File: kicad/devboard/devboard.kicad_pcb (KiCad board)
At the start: 2 copper layers, 4 parts, among them U2 CH340G, U3 STM32G030K8Tx

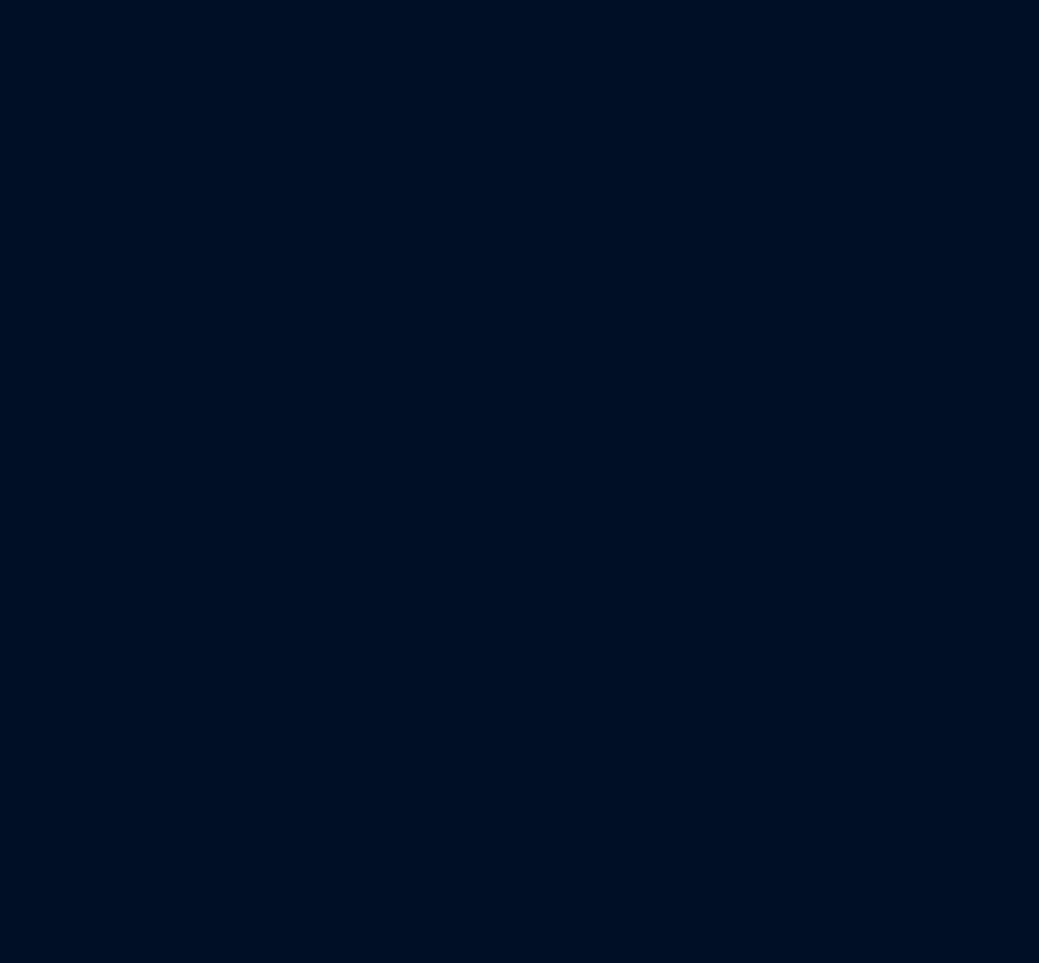
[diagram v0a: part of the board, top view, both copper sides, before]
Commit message: Added pin headers for SWD
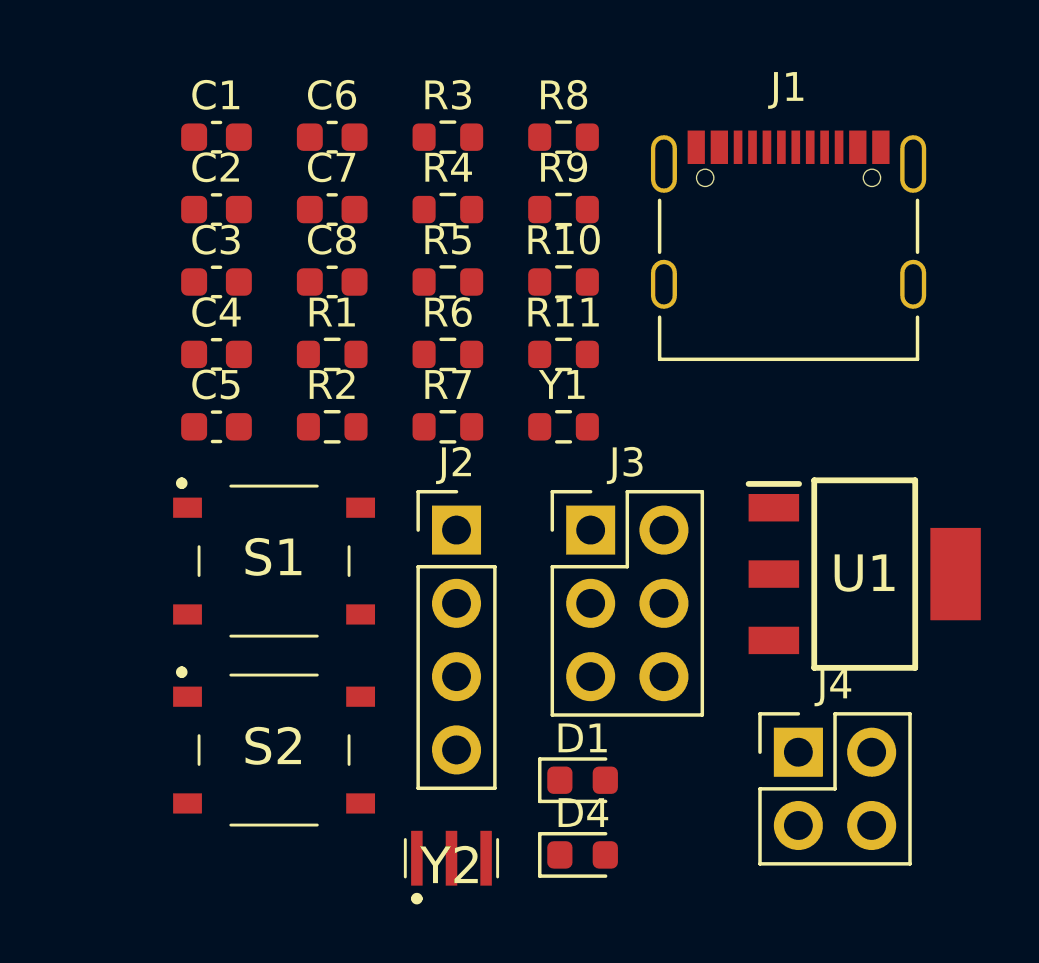
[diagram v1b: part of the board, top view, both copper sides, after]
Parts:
- added C1: 0.47 uF, Capacitor_SMD:C_0603_1608Metric, F.Cu at (138.3, 48.6)
- added C2: 33 uF, Capacitor_SMD:C_0603_1608Metric, F.Cu at (138.3, 51.1)
- added C3: 22 pF, Capacitor_SMD:C_0603_1608Metric, F.Cu at (138.3, 53.7)
- added C4: 22 pF, Capacitor_SMD:C_0603_1608Metric, F.Cu at (138.3, 56.2)
- added C5: 100 nF, Capacitor_SMD:C_0603_1608Metric, F.Cu at (138.3, 58.7)
- added C6: 0.1 uF, Capacitor_SMD:C_0603_1608Metric, F.Cu at (142.3, 48.6)
- added C7: 100 nF, Capacitor_SMD:C_0603_1608Metric, F.Cu at (142.3, 51.1)
- added C8: 100 nF, Capacitor_SMD:C_0603_1608Metric, F.Cu at (142.3, 53.7)
- added D1: LED, LED_SMD:LED_0603_1608Metric, F.Cu at (151.0, 70.9)
- added D4: LED, LED_SMD:LED_0603_1608Metric, F.Cu at (151.0, 73.5)
- added J1: USB_C_Receptacle, Connector_USB:USB_C_Receptacle_Palconn_UTC16-G, F.Cu at (158.1, 51.5)
- added J2: Conn_01x04_Socket, Connector_PinHeader_2.54mm:PinHeader_1x04_P2.54mm_Vertical, F.Cu at (146.6, 62.3)
- added J3: Conn_02x03_Top_Bottom, Connector_PinHeader_2.54mm:PinHeader_2x03_P2.54mm_Vertical, F.Cu at (151.3, 62.3)
- added J4: Conn_02x02_Top_Bottom, Connector_PinHeader_2.54mm:PinHeader_2x02_P2.54mm_Vertical, F.Cu at (158.5, 70.0)
- added R1: 1M, Resistor_SMD:R_0603_1608Metric, F.Cu at (142.3, 56.2)
- added R10: 10k, Resistor_SMD:R_0603_1608Metric, F.Cu at (150.3, 53.7)
- added R11: 10k, Resistor_SMD:R_0603_1608Metric, F.Cu at (150.3, 56.2)
- added R2: 1k, Resistor_SMD:R_0603_1608Metric, F.Cu at (142.3, 58.7)
- added R3: 470, Resistor_SMD:R_0603_1608Metric, F.Cu at (146.3, 48.6)
- added R4: 10k, Resistor_SMD:R_0603_1608Metric, F.Cu at (146.3, 51.1)
- added R5: 603, Resistor_SMD:R_0603_1608Metric, F.Cu at (146.3, 53.7)
- added R6: 5k1, Resistor_SMD:R_0603_1608Metric, F.Cu at (146.3, 56.2)
- added R7: 5k1, Resistor_SMD:R_0603_1608Metric, F.Cu at (146.3, 58.7)
- added R8: 1k, Resistor_SMD:R_0603_1608Metric, F.Cu at (150.3, 48.6)
- added R9: 1k, Resistor_SMD:R_0603_1608Metric, F.Cu at (150.3, 51.1)
- added S1: ~, mesonlib:PTS526SM15SMTR2LFS, F.Cu at (140.3, 63.3)
- added S2: ~, mesonlib:PTS526SM15SMTR2LFS, F.Cu at (140.3, 69.9)
- added U1: LM3940, mesonlib:LM3940, F.Cu at (160.8, 63.8)
- added Y1: 12 MHz, Resistor_SMD:R_0603_1608Metric, F.Cu at (150.3, 58.7)
- added Y2: 8 MHz, mesonlib:CSTNE16M0V530000R0, F.Cu at (146.4, 74.1)
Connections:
- U3 pad 19: Net-(U2-TXD) -> /TX-M
- U3 pad 21: Net-(U2-RXD) -> /RX-M
- U3 pad 24: unconnected-(U3-PA13-Pad24) -> /SWDIO

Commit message: All footprints done?
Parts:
- added C9: EEU-FR1V330, mesonlib:EEU-FR1330, F.Cu at (125.5, 85.3)
- added TH1: Thermistor_PTC, mesonlib:Eaton PTS120616V025, F.Cu at (135.5, 89.0)
- D1, D4, J1, S1, S2: moved to B.Cu
- Y1: footprint Resistor_SMD:R_0603_1608Metric -> Crystal:Crystal_SMD_HC49-SD
- moved Y1 28.3 mm to (178.6, 58.4)
- moved U1 16.7 mm to (177.2, 66.5)
- moved J3 9.94 mm to (159.7, 67.5)
- moved J4 9.35 mm to (159.7, 79.2)
- moved S1 8.37 mm to (132.0, 64.5), turned to 180 degrees
- moved Y2 7.61 mm to (144.5, 81.4)
- moved S2 7.02 mm to (135.0, 74.5), turned to 180 degrees
- moved D1 6.08 mm to (153.7, 65.5), turned to 180 degrees
- moved D4 4.27 mm to (154.0, 70.5), turned to 180 degrees
- moved J2 4.19 mm to (150.5, 60.7)
- moved J1 4.13 mm to (162.2, 50.8), turned to 180 degrees
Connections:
- net /BOOT renamed /SWCLK/BOOT

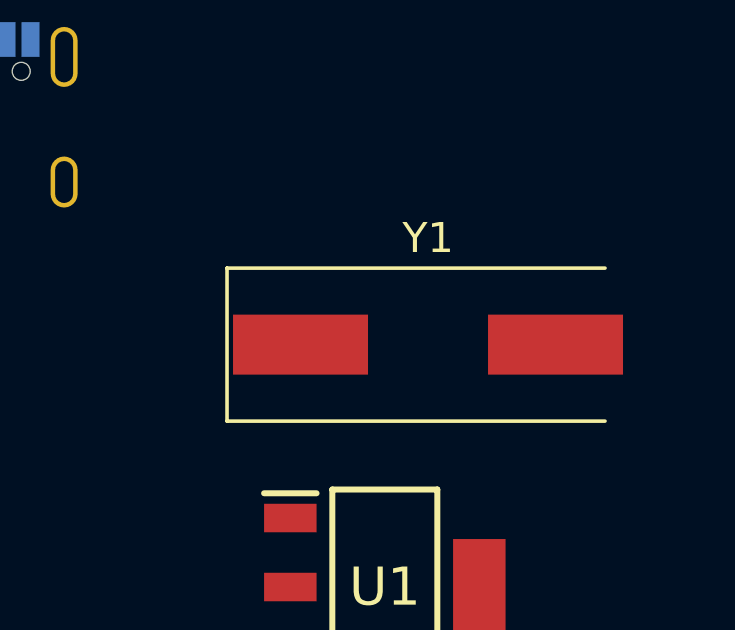
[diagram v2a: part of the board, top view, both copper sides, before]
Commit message: Added new 16-pin USB C symbol, updated PCB
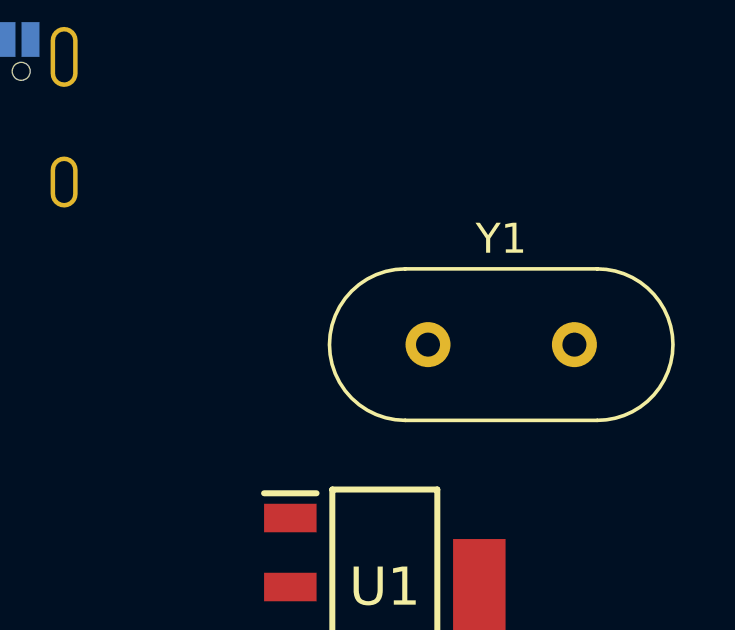
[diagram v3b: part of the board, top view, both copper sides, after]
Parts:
- Y1: footprint Crystal:Crystal_SMD_HC49-SD -> Crystal:Crystal_HC49-4H_Vertical
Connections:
- U1 pad 4: (no net) -> GND
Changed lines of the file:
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@@
 		)
 	)
-	(footprint "Crystal:Crystal_SMD_HC49-SD"
+	(footprint "Crystal:Crystal_HC49-4H_Vertical"
 		(layer "F.Cu")
 		(at 178.63 58.42)
-		(descr "SMD Crystal HC-49-SD http://cdn-reichelt.de/documents/datenblatt/B400/xxx-HC49-SMD.pdf, 11.4x4.7mm^2 package")
-		(tags "SMD SMT crystal")
+		(descr "Crystal THT HC-49-4H http://5hertz.com/pdfs/04404_D.pdf")
+		(tags "THT crystalHC-49-4H")
 		(property "Reference" "Y1"
-			(at 0 -3.55 0)
+			(at 2.44 -3.525 0)
 			(layer "F.SilkS")
 			(effects
@@
 		)
 		(property "Value" "12 MHz	"
-			(at 0 3.55 0)
+			(at 2.44 3.525 0)
 			(layer "F.Fab")
 			(effects
@@
 			)
 		)
-		(property "Footprint" "Crystal:Crystal_SMD_HC49-SD"
+		(property "Footprint" "Crystal:Crystal_HC49-4H_Vertical"
 			(at 0 0 0)
 			(unlocked yes)
@@
 		(sheetname "Root")
 		(sheetfile "devboard.kicad_sch")
-		(attr smd)
+		(attr through_hole)
 		(fp_line
-			(start -6.7 -2.55)
-			(end -6.7 2.55)
+			(start -0.76 -2.525)
+			(end 5.64 -2.525)
 			(stroke
 				(width 0.12)
@@
 		)
 		(fp_line
-			(start -6.7 2.55)
-			(end 5.9 2.55)
+			(start -0.76 2.525)
+			(end 5.64 2.525)
 			(stroke
 				(width 0.12)
@@
 			(layer "F.SilkS")
 		)
-		(fp_line
-			(start 5.9 -2.55)
-			(end -6.7 -2.55)
+		(fp_arc
+			(start -0.76 2.525)
+			(mid -3.285 0)
+			(end -0.76 -2.525)
+			(stroke
+				(width 0.12)
+				(type solid)
+			)
+			(layer "F.SilkS")
+		)
+		(fp_arc
+			(start 5.64 -2.525)
+			(mid 8.165 0)
+			(end 5.64 2.525)
 			(stroke
 				(width 0.12)
@@
 		)
 		(fp_line
-			(start -6.8 -2.6)
-			(end -6.8 2.6)
+			(start -3.6 -2.8)
+			(end -3.6 2.8)
 			(stroke
 				(width 0.05)
@@
 		)
 		(fp_line
-			(start -6.8 2.6)
-			(end 6.8 2.6)
+			(start -3.6 2.8)
+			(end 8.5 2.8)
 			(stroke
 				(width 0.05)
@@
 		)
 		(fp_line
-			(start 6.8 -2.6)
-			(end -6.8 -2.6)
+			(start 8.5 -2.8)
+			(end -3.6 -2.8)
 			(stroke
 				(width 0.05)
@@
 		)
 		(fp_line
-			(start 6.8 2.6)
-			(end 6.8 -2.6)
+			(start 8.5 2.8)
+			(end 8.5 -2.8)
 			(stroke
 				(width 0.05)
@@
 		)
 		(fp_line
-			(start -5.7 -2.35)
-			(end -5.7 2.35)
+			(start -0.76 -2.325)
+			(end 5.64 -2.325)
 			(stroke
 				(width 0.1)
@@
 		)
 		(fp_line
-			(start -5.7 2.35)
-			(end 5.7 2.35)
+			(start -0.76 2.325)
+			(end 5.64 2.325)
 			(stroke
 				(width 0.1)
@@
 		)
 		(fp_line
-			(start -3.015 -2.115)
-			(end 3.015 -2.115)
+			(start -0.56 -2)
+			(end 5.44 -2)
 			(stroke
 				(width 0.1)
@@
 		)
 		(fp_line
-			(start -3.015 2.115)
-			(end 3.015 2.115)
+			(start -0.56 2)
+			(end 5.44 2)
 			(stroke
 				(width 0.1)
@@
 			(layer "F.Fab")
 		)
-		(fp_line
-			(start 5.7 -2.35)
-			(end -5.7 -2.35)
+		(fp_arc
+			(start -0.76 2.325)
+			(mid -3.085 0)
+			(end -0.76 -2.325)
 			(stroke
 				(width 0.1)
@@
 			(layer "F.Fab")
 		)
-		(fp_line
-			(start 5.7 2.35)
-			(end 5.7 -2.35)
+		(fp_arc
+			(start -0.56 2)
+			(mid -2.56 0)
+			(end -0.56 -2)
 			(stroke
 				(width 0.1)
@@
 		)
 		(fp_arc
-			(start -3.015 2.115)
-			(mid -5.13 0)
-			(end -3.015 -2.115)
+			(start 5.44 -2)
+			(mid 7.44 0)
+			(end 5.44 2)
 			(stroke
 				(width 0.1)
@@
 		)
 		(fp_arc
-			(start 3.015 -2.115)
-			(mid 5.13 0)
-			(end 3.015 2.115)
+			(start 5.64 -2.325)
+			(mid 7.965 0)
+			(end 5.64 2.325)
 			(stroke
 				(width 0.1)
@@
 		)
 		(fp_text user "${REFERENCE}"
-			(at 0 0 0)
+			(at 2.44 0 0)
 			(layer "F.Fab")
 			(effects
@@
 			)
 		)
-		(pad "1" smd rect
-			(at -4.25 0)
-			(size 4.5 2)
-			(layers "F.Cu" "F.Paste" "F.Mask")
+		(pad "1" thru_hole circle
+			(at 0 0)
+			(size 1.5 1.5)
+			(drill 0.8)
+			(layers "*.Cu" "*.Mask")
+			(remove_unused_layers no)
 			(net 19 "Net-(U2-XI)")
 			(pinfunction "1")
 			(pintype "passive")
 		)
-		(pad "2" smd rect
-			(at 4.25 0)
-			(size 4.5 2)
-			(layers "F.Cu" "F.Paste" "F.Mask")
+		(pad "2" thru_hole circle
+			(at 4.88 0)
+			(size 1.5 1.5)
+			(drill 0.8)
+			(layers "*.Cu" "*.Mask")
+			(remove_unused_layers no)
 			(net 8 "Net-(U2-XO)")
 			(pinfunction "2")
 			(pintype "passive")
 		)
-		(model "${KICAD8_3DMODEL_DIR}/Crystal.3dshapes/Crystal_SMD_HC49-SD.wrl"
+		(model "${KICAD8_3DMODEL_DIR}/Crystal.3dshapes/Crystal_HC49-4H_Vertical.wrl"
 			(offset
 				(xyz 0 0 0)
@@
 			(size 1.75 3.2)
 			(layers "F.Cu" "F.Paste" "F.Mask")
+			(net 3 "GND")
+			(pintype "passive")
 			(thermal_bridge_angle 45)
 		)
@@
 		(tags "LED")
 		(property "Reference" "D1"
-			(at 0 1.43 -180)
+			(at 0 1.43 180)
 			(layer "B.SilkS")
 			(effects

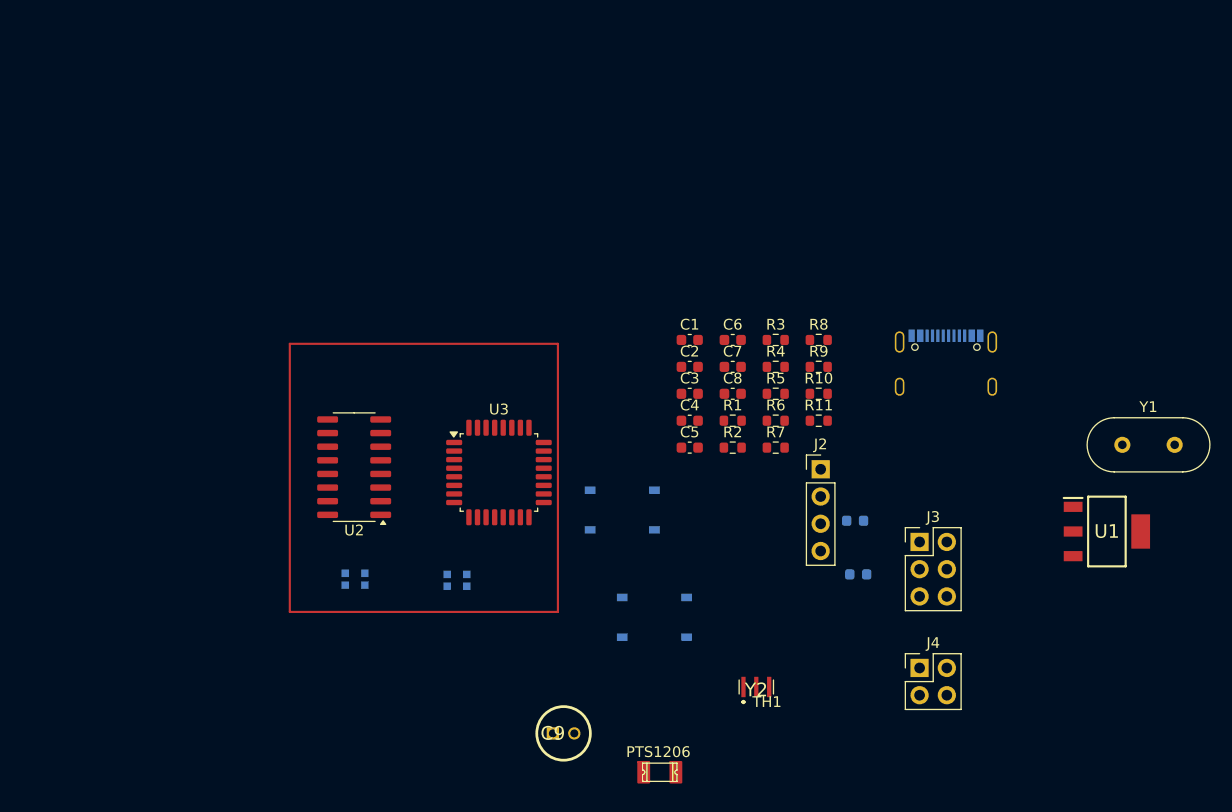
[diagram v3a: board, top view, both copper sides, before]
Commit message: Try placing more components on the board
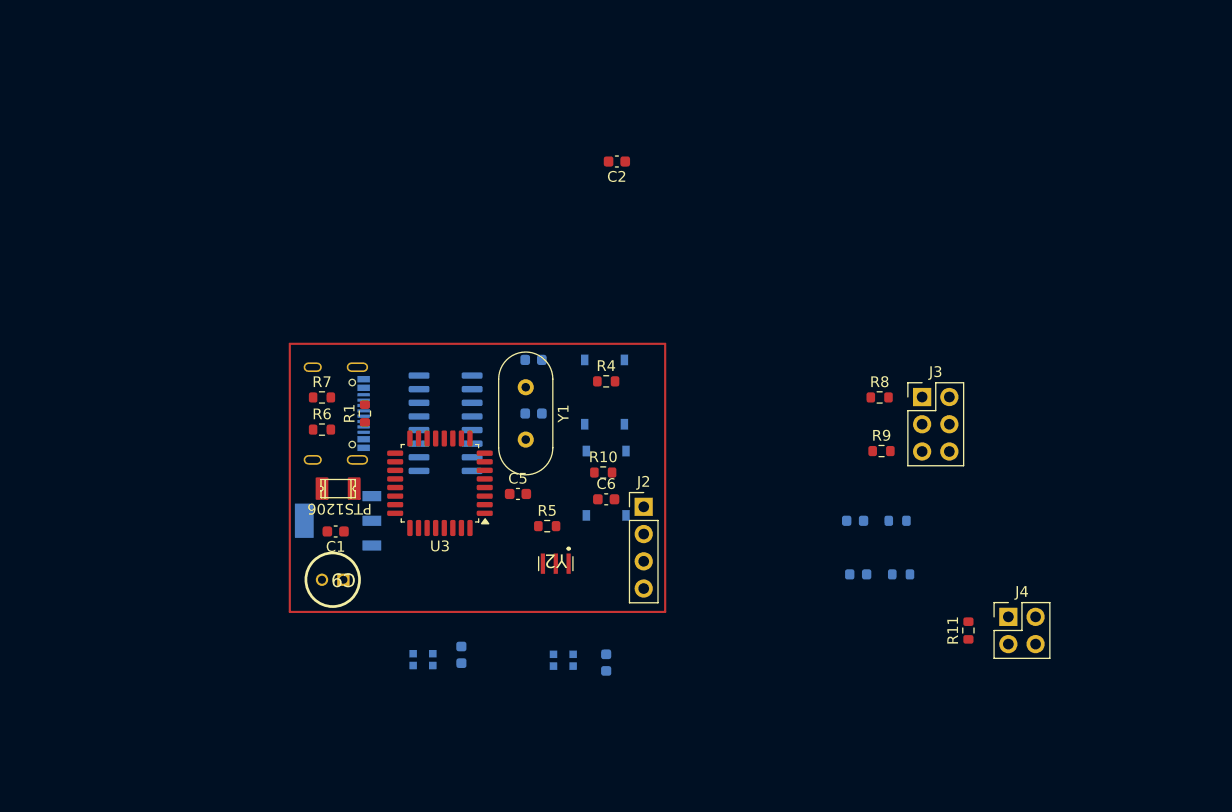
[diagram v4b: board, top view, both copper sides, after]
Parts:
- C3, C4, C7, C8, R2, R3, U1, U2: moved to B.Cu
- moved U1 71.7 mm to (105.5, 65.5), turned to 180 degrees
- moved J1 57.0 mm to (105.4, 55.5), turned to 90 degrees
- moved Y1 55.9 mm to (123.0, 53.0), turned to -90 degrees
- moved R7 42.6 mm to (104.0, 54.0)
- moved R6 42.3 mm to (104.0, 57.0)
- moved TH1 40.1 mm to (105.5, 62.5), turned to 180 degrees
- moved C1 37.5 mm to (105.3, 66.5), turned to 180 degrees
- moved C8 35.1 mm to (117.0, 78.0), turned to 90 degrees
- moved R1 34.3 mm to (108.0, 55.5), turned to 90 degrees
- moved C7 30.0 mm to (130.5, 78.7), turned to -90 degrees
- moved R3 24.8 mm to (158.0, 70.5)
- moved R5 24.6 mm to (125.0, 66.0)
- moved C9 24.2 mm to (106.0, 71.0), turned to 180 degrees
- moved R11 24.0 mm to (164.3, 75.7), turned to 90 degrees
- moved Y2 22.4 mm to (125.8, 69.1), turned to 180 degrees
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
